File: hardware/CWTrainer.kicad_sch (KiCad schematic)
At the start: 22 parts, among them J1 Analog, J2 Digital, J3 CW Out, J4 CW paddle in, J5 Headphones, J6 CW Paddle out, Q1 BC547, SW5 CW Paddle, U1 LCD1602-I2C, U2 pam8403

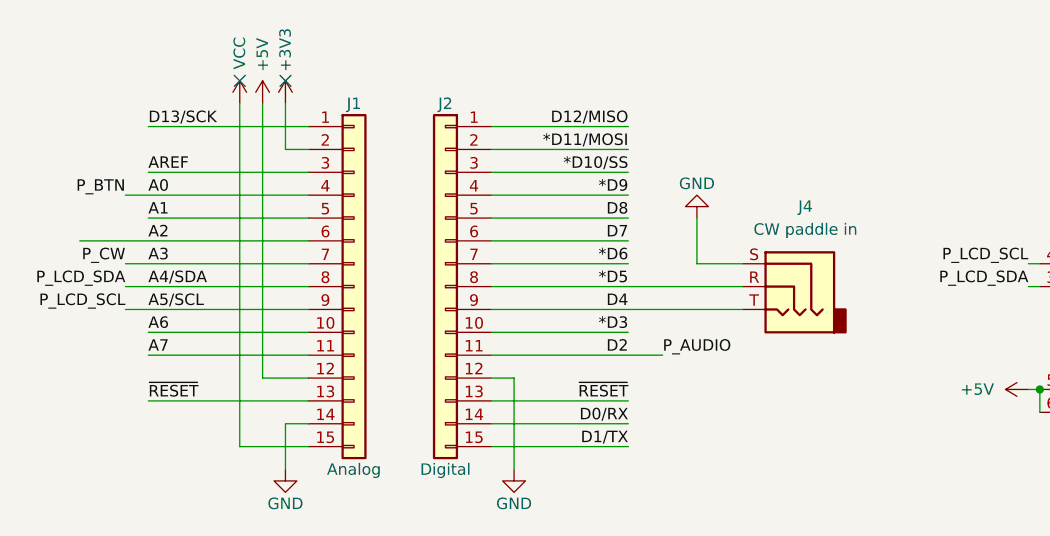
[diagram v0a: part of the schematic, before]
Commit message: RC2
подключен вывод на транссивер
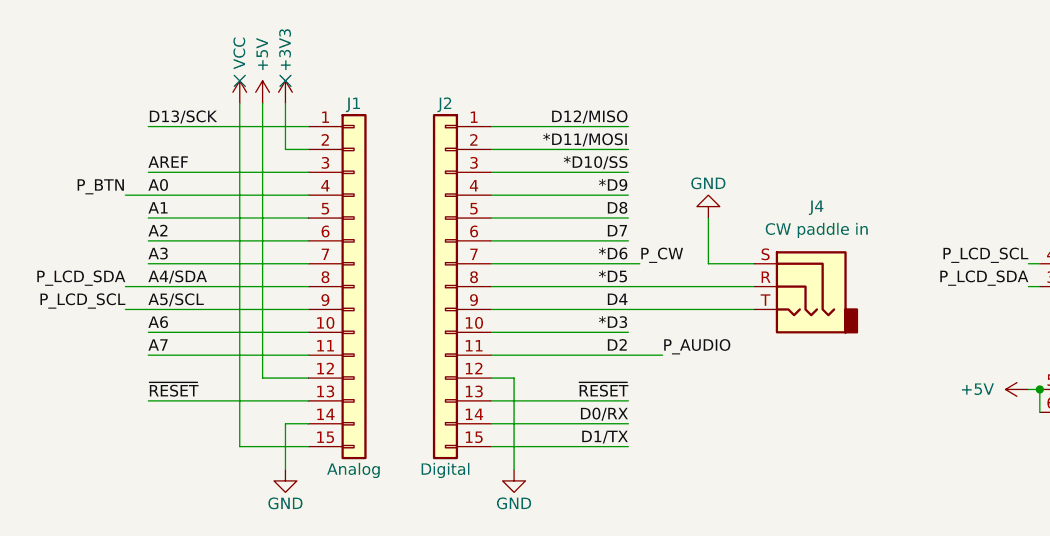
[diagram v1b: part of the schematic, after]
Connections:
- net *D6: now also R6.1
- net A3: no longer R6.1
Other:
- moved on the sheet: J4
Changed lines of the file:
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@@
 	(wire
 		(pts
-			(xy 91.44 39.37) (xy 91.44 44.45)
+			(xy 92.71 39.37) (xy 92.71 44.45)
 		)
 		(stroke
@@
 	(wire
 		(pts
-			(xy 27.94 44.45) (xy 48.26 44.45)
+			(xy 68.58 34.29) (xy 83.82 34.29)
 		)
 		(stroke
@@
 	(wire
 		(pts
-			(xy 68.58 34.29) (xy 83.82 34.29)
+			(xy 30.48 41.91) (xy 48.26 41.91)
 		)
 		(stroke
 			(width 0)
-			(type solid)
+			(type default)
 		)
 	)
@@
 	(wire
 		(pts
-			(xy 68.58 41.91) (xy 83.82 41.91)
-		)
-		(stroke
-			(width 0)
-			(type solid)
-		)
-	)
-	(wire
-		(pts
 			(xy 128.27 58.42) (xy 129.54 58.42)
 		)
@@
 	(wire
 		(pts
-			(xy 96.52 44.45) (xy 91.44 44.45)
+			(xy 97.79 44.45) (xy 92.71 44.45)
 		)
 		(stroke
@@
 	(wire
 		(pts
-			(xy 68.58 46.99) (xy 96.52 46.99)
+			(xy 68.58 46.99) (xy 97.79 46.99)
 		)
 		(stroke
@@
 	(wire
 		(pts
-			(xy 68.58 44.45) (xy 83.82 44.45)
+			(xy 68.58 44.45) (xy 85.09 44.45)
 		)
 		(stroke
@@
 	(wire
 		(pts
-			(xy 68.58 49.53) (xy 96.52 49.53)
+			(xy 68.58 49.53) (xy 97.79 49.53)
 		)
 		(stroke
@@
 	(wire
 		(pts
-			(xy 22.86 41.91) (xy 48.26 41.91)
-		)
-		(stroke
-			(width 0)
-			(type solid)
-		)
-	)
-	(wire
-		(pts
 			(xy 30.48 29.21) (xy 48.26 29.21)
 		)
@@
 	(wire
 		(pts
+			(xy 68.58 41.91) (xy 83.82 41.91)
+		)
+		(stroke
+			(width 0)
+			(type default)
+		)
+	)
+	(wire
+		(pts
 			(xy 30.48 39.37) (xy 48.26 39.37)
 		)
@@
 	(wire
 		(pts
+			(xy 30.48 44.45) (xy 48.26 44.45)
+		)
+		(stroke
+			(width 0)
+			(type default)
+		)
+	)
+	(wire
+		(pts
 			(xy 45.72 97.79) (xy 45.72 99.06)
 		)
@@
 	)
 	(label "P_CW"
-		(at 27.94 44.45 180)
+		(at 85.09 44.45 0)
 		(effects
 			(font
 				(size 1.27 1.27)
 			)
-			(justify right bottom)
+			(justify left bottom)
 		)
 	)
@@
 	(symbol
 		(lib_id "Connector_Audio:AudioJack3")
-		(at 101.6 46.99 0)
+		(at 102.87 46.99 0)
 		(mirror y)
 		(unit 1)
@@
 		(dnp no)
 		(property "Reference" "J4"
-			(at 103.505 38.1 0)
+			(at 104.775 38.1 0)
 			(show_name no)
 			(do_not_autoplace no)
@@
 		)
 		(property "Value" "CW paddle in"
-			(at 103.505 40.64 0)
+			(at 104.775 40.64 0)
 			(show_name no)
 			(do_not_autoplace no)
@@
 		)
 		(property "Footprint" ""
-			(at 101.6 46.99 0)
+			(at 102.87 46.99 0)
 			(hide yes)
 			(show_name no)
@@
 		)
 		(property "Datasheet" ""
-			(at 101.6 46.99 0)
+			(at 102.87 46.99 0)
 			(hide yes)
 			(show_name no)
@@
 		)
 		(property "Description" "Audio Jack, 3 Poles (Stereo / TRS)"
-			(at 101.6 46.99 0)
+			(at 102.87 46.99 0)
 			(hide yes)
 			(show_name no)
@@
 	(symbol
 		(lib_id "power:GND")
-		(at 91.44 39.37 0)
+		(at 92.71 39.37 0)
 		(mirror x)
 		(unit 1)
@@
 		(dnp no)
 		(property "Reference" "#PWR0109"
-			(at 91.44 33.02 0)
+			(at 92.71 33.02 0)
 			(hide yes)
 			(show_name no)
@@
 		)
 		(property "Value" "GND"
-			(at 91.44 35.56 0)
+			(at 92.71 35.56 0)
 			(show_name no)
 			(do_not_autoplace no)
@@
 		)
 		(property "Footprint" ""
-			(at 91.44 39.37 0)
+			(at 92.71 39.37 0)
 			(hide yes)
 			(show_name no)
@@
 		)
 		(property "Datasheet" ""
-			(at 91.44 39.37 0)
+			(at 92.71 39.37 0)
 			(hide yes)
 			(show_name no)
@@
 		)
 		(property "Description" "Power symbol creates a global label with name \"GND\" , ground"
-			(at 91.44 39.37 0)
+			(at 92.71 39.37 0)
 			(hide yes)
 			(show_name no)
